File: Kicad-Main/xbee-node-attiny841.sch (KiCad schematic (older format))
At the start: 39 parts, among them P10 CONN_1, P11 CONN_1, P12 CONN_1, P13 CONN_1, P14 CONN_1, P15 CONN_1, P16 CONN_1, P17 CONN_1, P18 CONN_1, P19 CONN_1, P2 XBee Adaptor, P20 CONN_1, P3 Debug Adaptor, P7 CONN_1, P8 CONN_1, P9 CONN_1, Q2 MMBT3904, Q3 2N7002, U1 ATTINY841, U2 MAX952ESA, U3 TPS77033

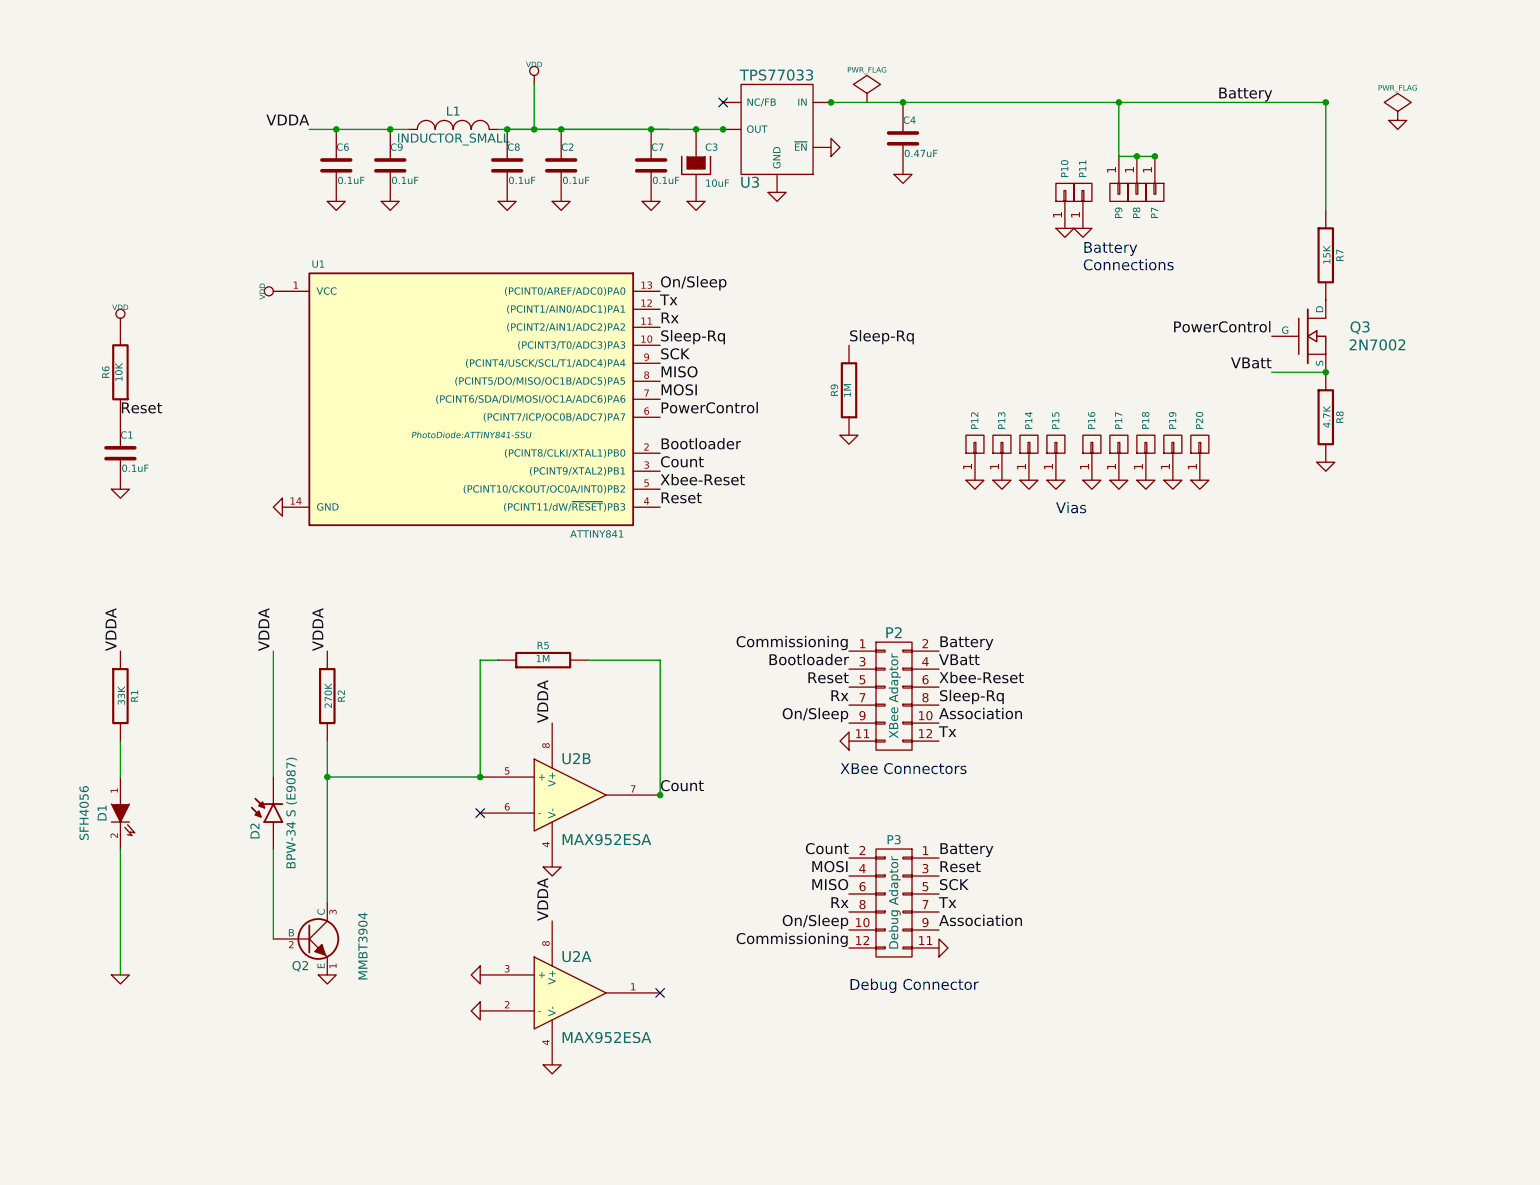
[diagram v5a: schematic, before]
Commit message: Update Main board PCB to modify battery monitor circuit.
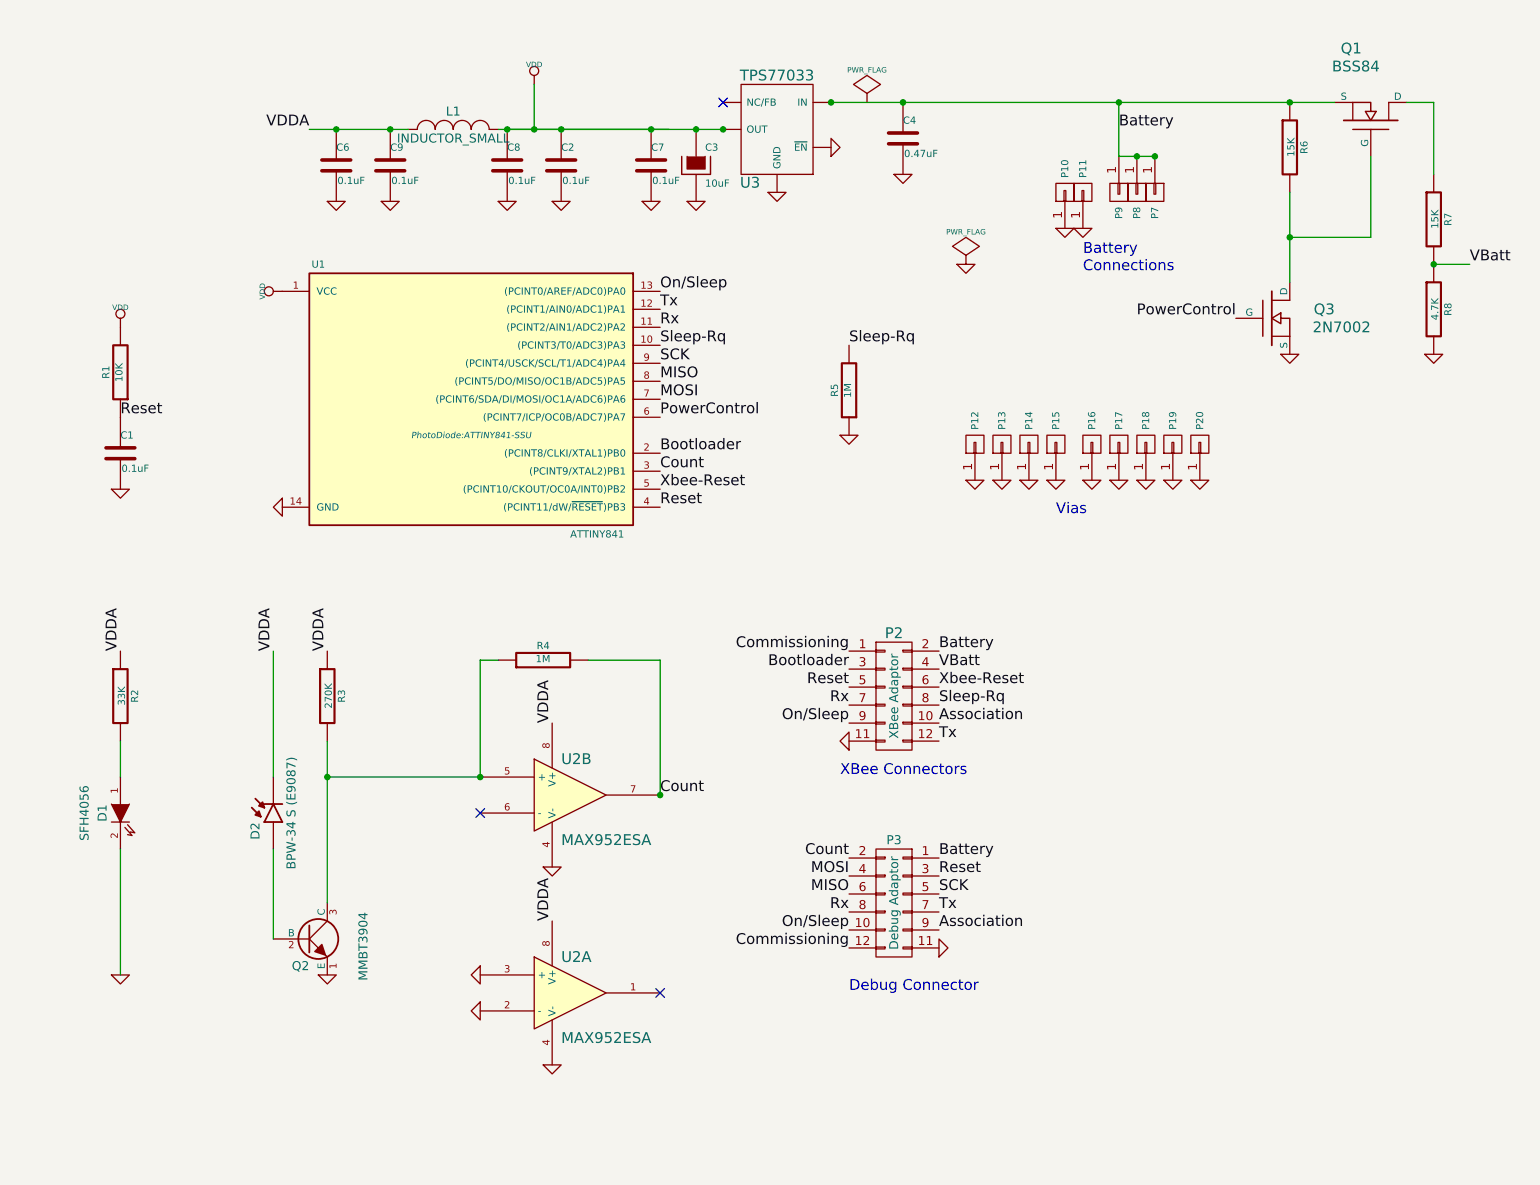
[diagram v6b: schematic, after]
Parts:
- added Q1: BSS84, PhotoDiode:SOT23GDS, symbol MOSFET_N-RESCUE-xbee-node-attiny841
- added R6: 15K, PhotoDiode:SM0603_Resistor, symbol R-RESCUE-xbee-node-attiny841
- renumbered R6 to R1, R1 to R2, R2 to R3, R5 to R4, R9 to R5
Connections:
- wire segments 19 -> 23
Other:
- moved on the sheet: Q3, R7, R8
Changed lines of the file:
@@
 L MOSFET_N-RESCUE-xbee-node-attiny841 Q3
 U 1 1 53D32AE5
-P 9550 2700
-F 0 "Q3" H 9900 2750 60  0000 R CNN
-F 1 "2N7002" H 10100 2650 60  0000 R CNN
-F 2 "PhotoDiode:SOT23GDS" H 9550 2700 60  0001 C CNN
-F 3 "" H 9550 2700 60  0000 C CNN
-	1    9550 2700
+P 9350 2600
+F 0 "Q3" H 9700 2650 60  0000 R CNN
+F 1 "2N7002" H 9900 2550 60  0000 R CNN
+F 2 "PhotoDiode:SOT23GDS" H 9350 2600 60  0001 C CNN
+F 3 "" H 9350 2600 60  0000 C CNN
+	1    9350 2600
 	1    0    0    -1
 $EndComp
@@
 L R-RESCUE-xbee-node-attiny841 R7
 U 1 1 53D32AFA
-P 9650 2250
-F 0 "R7" V 9730 2250 40  0000 C CNN
-F 1 "15K" V 9657 2251 40  0000 C CNN
-F 2 "PhotoDiode:SM0603_Resistor" V 9580 2250 30  0001 C CNN
-F 3 "" H 9650 2250 30  0000 C CNN
-	1    9650 2250
+P 10250 2050
+F 0 "R7" V 10330 2050 40  0000 C CNN
+F 1 "15K" V 10257 2051 40  0000 C CNN
+F 2 "PhotoDiode:SM0603_Resistor" V 10180 2050 30  0001 C CNN
+F 3 "" H 10250 2050 30  0000 C CNN
+	1    10250 2050
 	1    0    0    -1
 $EndComp
@@
 L R-RESCUE-xbee-node-attiny841 R8
 U 1 1 53D32B0E
-P 9650 3150
-F 0 "R8" V 9730 3150 40  0000 C CNN
-F 1 "4.7K" V 9657 3151 40  0000 C CNN
-F 2 "PhotoDiode:SM0603_Resistor" V 9580 3150 30  0001 C CNN
-F 3 "" H 9650 3150 30  0000 C CNN
-	1    9650 3150
-	1    0    0    -1
-$EndComp
-$Comp
-L R-RESCUE-xbee-node-attiny841 R6
+P 10250 2550
+F 0 "R8" V 10330 2550 40  0000 C CNN
+F 1 "4.7K" V 10257 2551 40  0000 C CNN
+F 2 "PhotoDiode:SM0603_Resistor" V 10180 2550 30  0001 C CNN
+F 3 "" H 10250 2550 30  0000 C CNN
+	1    10250 2550
+	1    0    0    -1
+$EndComp
+$Comp
+L R-RESCUE-xbee-node-attiny841 R1
 U 1 1 53D32B68
 P 2950 2900
-F 0 "R6" V 3030 2900 40  0000 C CNN
+F 0 "R1" V 3030 2900 40  0000 C CNN
 F 1 "10K" V 2957 2901 40  0000 C CNN
 F 2 "PhotoDiode:SM0603_Resistor" V 2880 2900 30  0001 C CNN
@@
 L GND-RESCUE-xbee-node-attiny841 #PWR07
 U 1 1 53D331C5
-P 9650 3400
-F 0 "#PWR07" H 9650 3400 30  0001 C CNN
-F 1 "GND" H 9650 3330 30  0001 C CNN
-F 2 "" H 9650 3400 60  0000 C CNN
-F 3 "" H 9650 3400 60  0000 C CNN
-	1    9650 3400
+P 9450 2800
+F 0 "#PWR07" H 9450 2800 30  0001 C CNN
+F 1 "GND" H 9450 2730 30  0001 C CNN
+F 2 "" H 9450 2800 60  0000 C CNN
+F 3 "" H 9450 2800 60  0000 C CNN
+	1    9450 2800
 	1    0    0    -1
 $EndComp
@@
 $EndComp
 $Comp
-L R-RESCUE-xbee-node-attiny841 R5
+L R-RESCUE-xbee-node-attiny841 R4
 U 1 1 53D35C63
 P 5300 4500
-F 0 "R5" V 5380 4500 40  0000 C CNN
+F 0 "R4" V 5380 4500 40  0000 C CNN
 F 1 "1M" V 5307 4501 40  0000 C CNN
 F 2 "PhotoDiode:SM0603_Resistor" V 5230 4500 30  0001 C CNN
@@
 $EndComp
 $Comp
-L R-RESCUE-xbee-node-attiny841 R2
+L R-RESCUE-xbee-node-attiny841 R3
 U 1 1 53D35F1D
 P 4100 4700
-F 0 "R2" V 4180 4700 40  0000 C CNN
+F 0 "R3" V 4180 4700 40  0000 C CNN
 F 1 "270K" V 4107 4701 40  0000 C CNN
 F 2 "PhotoDiode:SM0603_Resistor" V 4030 4700 30  0001 C CNN
@@
 $EndComp
 $Comp
-L R-RESCUE-xbee-node-attiny841 R1
+L R-RESCUE-xbee-node-attiny841 R2
 U 1 1 53DCC4A4
 P 2950 4700
-F 0 "R1" V 3030 4700 40  0000 C CNN
+F 0 "R2" V 3030 4700 40  0000 C CNN
 F 1 "33K" V 2957 4701 40  0000 C CNN
 F 2 "PhotoDiode:SM0603_Resistor" V 2880 4700 30  0001 C CNN
@@
 	1    0    0    -1
 $EndComp
-Text Label 9350 2900 2    60   ~ 0
+Text Label 10450 2300 0    60   ~ 0
 VBatt
 Text Label 7500 4550 0    60   ~ 0
@@
 L GND-RESCUE-xbee-node-attiny841 #PWR021
 U 1 1 53E26458
-P 10050 1500
-F 0 "#PWR021" H 10050 1500 30  0001 C CNN
-F 1 "GND" H 10050 1430 30  0001 C CNN
-F 2 "" H 10050 1500 60  0000 C CNN
-F 3 "" H 10050 1500 60  0000 C CNN
-	1    10050 1500
+P 7650 2300
+F 0 "#PWR021" H 7650 2300 30  0001 C CNN
+F 1 "GND" H 7650 2230 30  0001 C CNN
+F 2 "" H 7650 2300 60  0000 C CNN
+F 3 "" H 7650 2300 60  0000 C CNN
+	1    7650 2300
 	1    0    0    -1
 $EndComp
@@
 L PWR_FLAG #FLG022
 U 1 1 53E267FB
-P 10050 1500
-F 0 "#FLG022" H 10050 1595 30  0001 C CNN
-F 1 "PWR_FLAG" H 10050 1680 30  0000 C CNN
-F 2 "" H 10050 1500 60  0000 C CNN
-F 3 "" H 10050 1500 60  0000 C CNN
-	1    10050 1500
+P 7650 2300
+F 0 "#FLG022" H 7650 2395 30  0001 C CNN
+F 1 "PWR_FLAG" H 7650 2480 30  0000 C CNN
+F 2 "" H 7650 2300 60  0000 C CNN
+F 3 "" H 7650 2300 60  0000 C CNN
+	1    7650 2300
 	-1   0    0    -1
 $EndComp
@@
 Text Label 5950 3150 0    60   ~ 0
 PowerControl
-Text Label 9350 2700 2    60   ~ 0
+Text Label 9150 2600 2    60   ~ 0
 PowerControl
 $Comp
@@
 	1    0    0    -1
 $EndComp
-Text Label 9050 1400 0    60   ~ 0
+Text Label 8500 1550 0    60   ~ 0
 Battery
 Text Label 7500 5600 0    60   ~ 0
@@
 $EndComp
 $Comp
-L R-RESCUE-xbee-node-attiny841 R9
+L R-RESCUE-xbee-node-attiny841 R5
 U 1 1 54823620
 P 7000 3000
-F 0 "R9" V 7080 3000 40  0000 C CNN
+F 0 "R5" V 7080 3000 40  0000 C CNN
 F 1 "1M" V 7007 3001 40  0000 C CNN
 F 2 "PhotoDiode:SM0603_Resistor" V 6930 3000 30  0001 C CNN
@@
 	1    0    0    -1
 $EndComp
-Wire Wire Line
-	2950 4950 2950 5150
-Wire Wire Line
-	2950 5550 2950 6250
-Connection ~ 9650 1400
-Wire Wire Line
-	3800 4450 3800 5150
-Connection ~ 4100 5150
-Wire Wire Line
-	3800 5550 3800 6050
-Wire Wire Line
-	4100 4950 4100 5850
-Wire Wire Line
-	4950 5150 4950 4500
-Wire Wire Line
-	4100 5150 4950 5150
-Wire Wire Line
-	4950 4500 5050 4500
-Wire Wire Line
-	5950 4500 5550 4500
-Wire Wire Line
-	5950 5250 5950 4500
-Wire Wire Line
-	6900 1400 9650 1400
-Wire Wire Line
-	9650 1400 9650 2000
-Connection ~ 7300 1400
-Connection ~ 6150 1550
-Connection ~ 5900 1550
-Connection ~ 4450 1550
-Connection ~ 5400 1550
-Connection ~ 5950 5250
-Connection ~ 4950 5150
-Connection ~ 9650 2900
-Wire Wire Line
-	9650 2900 9350 2900
-Wire Wire Line
-	8500 1700 8700 1700
-Wire Wire Line
-	8500 1700 8500 1400
-Connection ~ 8500 1400
-Connection ~ 8700 1700
-Connection ~ 8600 1700
-Wire Wire Line
-	5050 1550 6300 1550
-Wire Wire Line
-	4000 1550 4550 1550
-Connection ~ 5100 1550
-Wire Wire Line
-	5100 1550 6000 1550
-Wire Wire Line
-	5250 1300 5250 1550
-Connection ~ 5250 1550
 Text Label 4000 1550 2    60   ~ 0
 VDDA
@@
 Text Label 5350 5950 1    60   ~ 0
 VDDA
-Connection ~ 4150 1550
 Text Label 3800 4450 1    60   ~ 0
 VDDA
@@
 Text Label 4100 4450 1    60   ~ 0
 VDDA
-Connection ~ 6900 1400
-Connection ~ 6300 1550
 Text Label 7500 4450 0    60   ~ 0
 Battery
@@
 	1    0    0    -1
 $EndComp
+$Comp
+L MOSFET_N-RESCUE-xbee-node-attiny841 Q1
+U 1 1 587F3C83
+P 9900 1500
+F 0 "Q1" V 10300 1450 60  0000 R CNN
+F 1 "BSS84" V 10200 1550 60  0000 R CNN
+F 2 "PhotoDiode:SOT23GDS" H 9900 1500 60  0001 C CNN
+F 3 "" H 9900 1500 60  0000 C CNN
+	1    9900 1500
+	0    1    -1   0
+$EndComp
+$Comp
+L R-RESCUE-xbee-node-attiny841 R6
+U 1 1 587F435F
+P 9450 1650
+F 0 "R6" V 9530 1650 40  0000 C CNN
+F 1 "15K" V 9457 1651 40  0000 C CNN
+F 2 "PhotoDiode:SM0603_Resistor" V 9380 1650 30  0001 C CNN
+F 3 "" H 9450 1650 30  0000 C CNN
+	1    9450 1650
+	1    0    0    -1
+$EndComp
+$Comp
+L GND-RESCUE-xbee-node-attiny841 #PWR039
+U 1 1 587F441B
+P 10250 2800
+F 0 "#PWR039" H 10250 2800 30  0001 C CNN
+F 1 "GND" H 10250 2730 30  0001 C CNN
+F 2 "" H 10250 2800 60  0000 C CNN
+F 3 "" H 10250 2800 60  0000 C CNN
+	1    10250 2800
+	1    0    0    -1
+$EndComp
+Wire Wire Line
+	2950 4950 2950 5150
+Wire Wire Line
+	2950 5550 2950 6250
+Connection ~ 9450 1400
+Wire Wire Line
+	3800 4450 3800 5150
+Connection ~ 4100 5150
+Wire Wire Line
+	3800 5550 3800 6050
+Wire Wire Line
+	4100 4950 4100 5850
+Wire Wire Line
+	4950 5150 4950 4500
+Wire Wire Line
+	4100 5150 4950 5150
+Wire Wire Line
+	4950 4500 5050 4500
+Wire Wire Line
+	5950 4500 5550 4500
+Wire Wire Line
+	5950 5250 5950 4500
+Connection ~ 7300 1400
+Connection ~ 6150 1550
+Connection ~ 5900 1550
+Connection ~ 4450 1550
+Connection ~ 5400 1550
+Connection ~ 5950 5250
+Connection ~ 4950 5150
+Connection ~ 10250 2300
+Wire Wire Line
+	8500 1700 8700 1700
+Wire Wire Line
+	8500 1400 8500 1700
+Connection ~ 8500 1400
+Connection ~ 8700 1700
+Connection ~ 8600 1700
+Wire Wire Line
+	5050 1550 6300 1550
+Wire Wire Line
+	4000 1550 4550 1550
+Connection ~ 5100 1550
+Wire Wire Line
+	5100 1550 6000 1550
+Wire Wire Line
+	5250 1300 5250 1550
+Connection ~ 5250 1550
+Connection ~ 4150 1550
+Connection ~ 6900 1400
+Connection ~ 6300 1550
+Wire Wire Line
+	6900 1400 9700 1400
+Wire Wire Line
+	9450 1900 9450 2400
+Wire Wire Line
+	10100 1400 10250 1400
+Wire Wire Line
+	10250 1400 10250 1800
+Wire Wire Line
+	9900 1700 9900 2150
+Wire Wire Line
+	9900 2150 9450 2150
+Connection ~ 9450 2150
+Wire Wire Line
+	10250 2300 10450 2300
 $EndSCHEMATC

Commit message: Kicad-Main, Kicad-Mounts and Kicad-Testboard. Add a range of symbol and footprint libraries and repair some problems apparently due to randomized changes in Kicad repository libraries.
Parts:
- removed L1: INDUCTOR_SMALL, PhotoDiode:R_0805, symbol INDUCTOR_SMALL
- added L1: 100nH, photodiode:R_0805, symbol L_Small
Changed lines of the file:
@@
 LIBS:TransistorParts
 LIBS:Sensors
-LIBS:xbee-node-attiny841-cache
 EELAYER 25 0
 EELAYER END
@@
 Text Label 7000 2750 0    60   ~ 0
 Sleep-Rq
-$Comp
-L INDUCTOR_SMALL L1
-U 1 1 548D0C86
-P 4800 1550
-F 0 "L1" H 4800 1650 50  0000 C CNN
-F 1 "INDUCTOR_SMALL" H 4800 1500 50  0000 C CNN
-F 2 "PhotoDiode:R_0805" H 4800 1550 60  0001 C CNN
-F 3 "" H 4800 1550 60  0000 C CNN
-	1    4800 1550
-	1    0    0    -1
-$EndComp
 $Comp
 L C-RESCUE-xbee-node-attiny841 C8
@@
 Connection ~ 8600 1700
 Wire Wire Line
-	5050 1550 6300 1550
-Wire Wire Line
-	4000 1550 4550 1550
+	4900 1550 6300 1550
+Wire Wire Line
+	4000 1550 4700 1550
 Connection ~ 5100 1550
 Wire Wire Line
@@
 Wire Wire Line
 	10250 2300 10450 2300
+$Comp
+L L_Small L1
+U 1 1 589058F4
+P 4800 1550
+F 0 "L1" V 4900 1500 50  0000 L CNN
+F 1 "100nH" V 4700 1450 50  0000 L CNN
+F 2 "photodiode:R_0805" H 4800 1550 50  0001 C CNN
+F 3 "" H 4800 1550 50  0000 C CNN
+	1    4800 1550
+	0    -1   -1   0
+$EndComp
 $EndSCHEMATC

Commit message: Minor tweaks on the PCBs ready to manufacture
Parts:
- added R9: 1M, PhotoDiode:SM0603_Resistor, symbol R-RESCUE-xbee-node-attiny841
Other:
- moved on the sheet: R5
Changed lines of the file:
@@
 LIBS:TransistorParts
 LIBS:Sensors
+LIBS:xbee-node-attiny841-cache
 EELAYER 25 0
 EELAYER END
@@
 L R-RESCUE-xbee-node-attiny841 R5
 U 1 1 54823620
-P 7000 3000
-F 0 "R5" V 7080 3000 40  0000 C CNN
-F 1 "1M" V 7007 3001 40  0000 C CNN
-F 2 "PhotoDiode:SM0603_Resistor" V 6930 3000 30  0001 C CNN
-F 3 "" H 7000 3000 30  0000 C CNN
-	1    7000 3000
+P 8850 4250
+F 0 "R5" V 8930 4250 40  0000 C CNN
+F 1 "1M" V 8857 4251 40  0000 C CNN
+F 2 "PhotoDiode:SM0603_Resistor" V 8780 4250 30  0001 C CNN
+F 3 "" H 8850 4250 30  0000 C CNN
+	1    8850 4250
 	-1   0    0    1
 $EndComp
@@
 L GND-RESCUE-xbee-node-attiny841 #PWR034
 U 1 1 5482395B
-P 7000 3250
-F 0 "#PWR034" H 7000 3250 30  0001 C CNN
-F 1 "GND" H 7000 3180 30  0001 C CNN
-F 2 "" H 7000 3250 60  0000 C CNN
-F 3 "" H 7000 3250 60  0000 C CNN
-	1    7000 3250
-	1    0    0    -1
-$EndComp
-Text Label 7000 2750 0    60   ~ 0
+P 8850 4500
+F 0 "#PWR034" H 8850 4500 30  0001 C CNN
+F 1 "GND" H 8850 4430 30  0001 C CNN
+F 2 "" H 8850 4500 60  0000 C CNN
+F 3 "" H 8850 4500 60  0000 C CNN
+	1    8850 4500
+	1    0    0    -1
+$EndComp
+Text Label 8850 4000 0    60   ~ 0
 Sleep-Rq
 $Comp
@@
 	0    -1   -1   0
 $EndComp
+$Comp
+L R-RESCUE-xbee-node-attiny841 R9
+U 1 1 589265FC
+P 9650 4250
+F 0 "R9" V 9730 4250 40  0000 C CNN
+F 1 "1M" V 9657 4251 40  0000 C CNN
+F 2 "PhotoDiode:SM0603_Resistor" V 9580 4250 30  0001 C CNN
+F 3 "" H 9650 4250 30  0000 C CNN
+	1    9650 4250
+	-1   0    0    1
+$EndComp
+$Comp
+L GND-RESCUE-xbee-node-attiny841 #PWR?
+U 1 1 589266AB
+P 9650 4500
+F 0 "#PWR?" H 9650 4500 30  0001 C CNN
+F 1 "GND" H 9650 4430 30  0001 C CNN
+F 2 "" H 9650 4500 60  0000 C CNN
+F 3 "" H 9650 4500 60  0000 C CNN
+	1    9650 4500
+	1    0    0    -1
+$EndComp
+Text Label 9650 4000 0    60   ~ 0
+PowerControl
 $EndSCHEMATC
